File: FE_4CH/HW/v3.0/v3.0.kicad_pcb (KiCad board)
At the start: 4 copper layers, 72 x 26 mm, 158 parts, among them J1 SMA-ANG, J2 PINH_2MM_2P, J3 USB4080-03-A, J6 MS300-10F, U1 MAX2771, U10 74AVC9112DCH, U11 PI3USB302-AZBEX, U2 MAX2771, U3 MAX2771, U4 MAX2771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

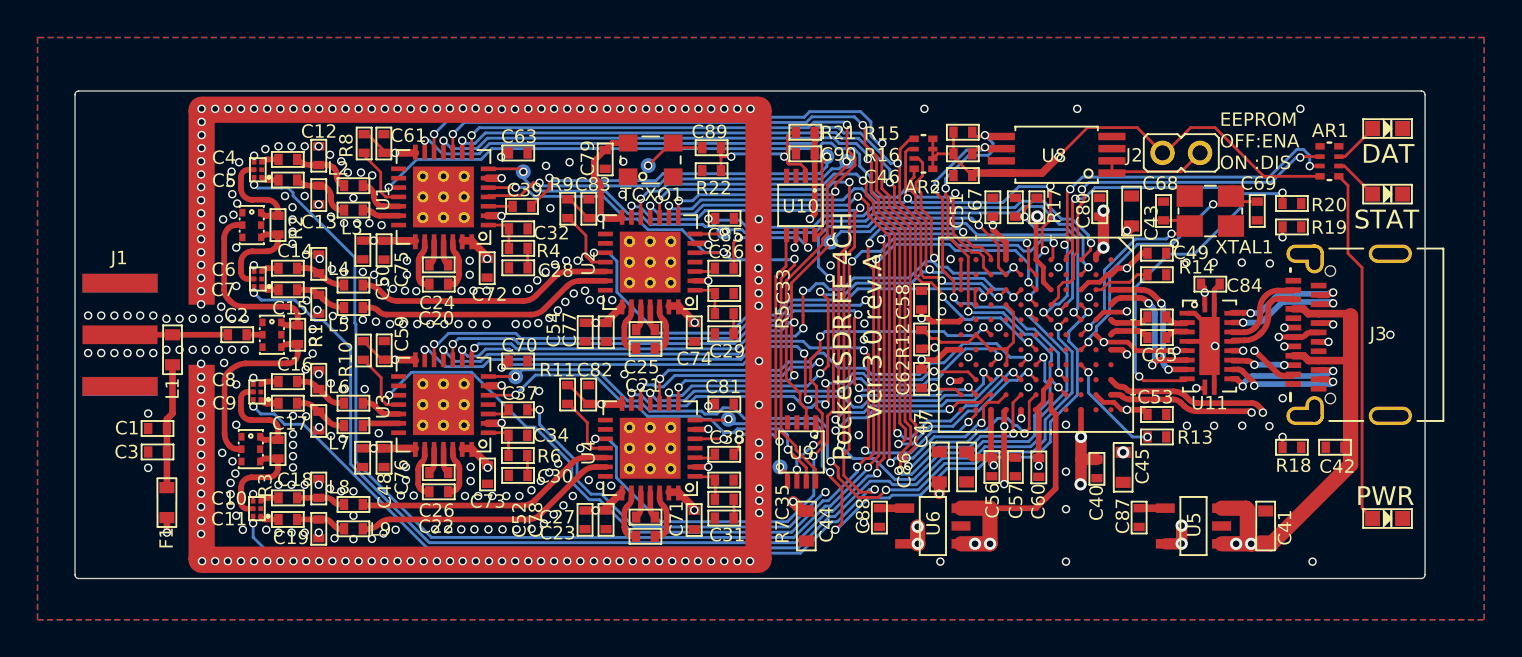
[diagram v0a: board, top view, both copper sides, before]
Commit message: replace wilkinson splitter with double, add mounting holes and fidushes
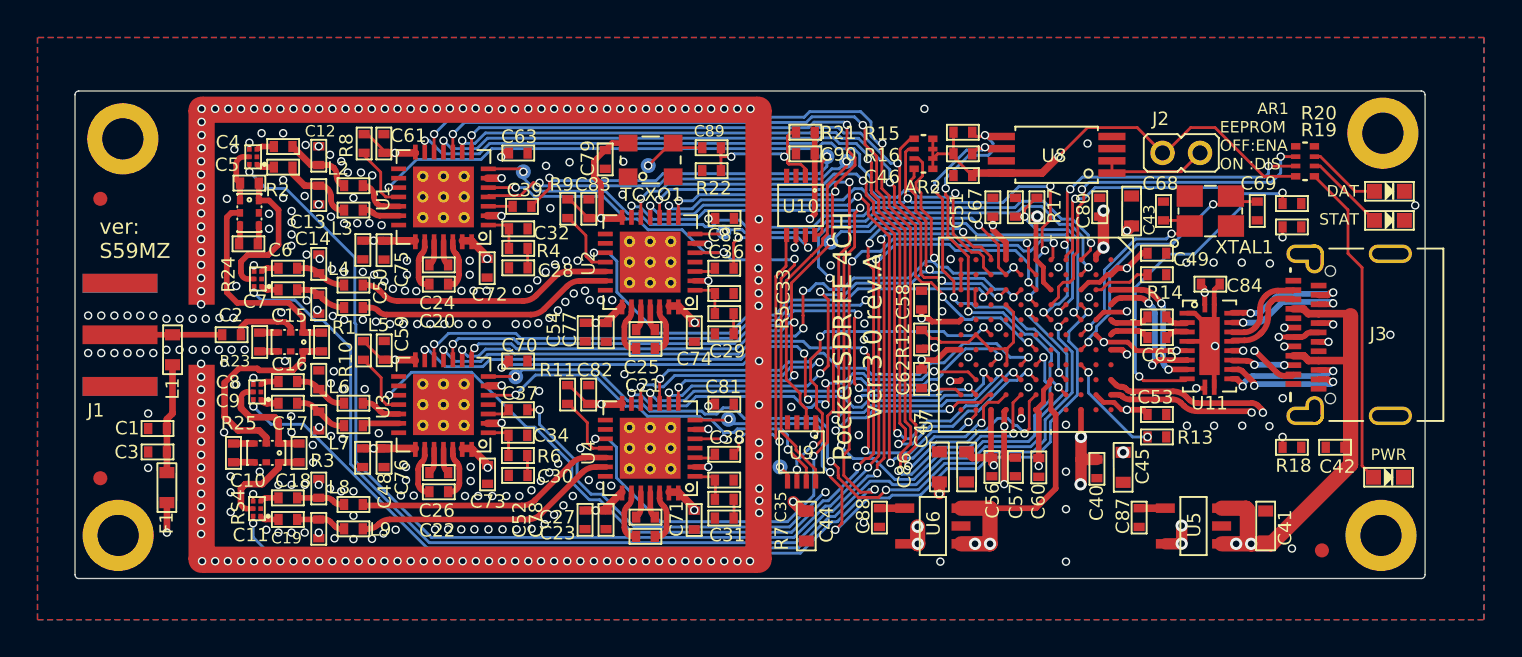
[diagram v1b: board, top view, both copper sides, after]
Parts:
- added FID1: Fiducial, Fiducial:Fiducial_0.75mm_Mask1.5mm, F.Cu at (122.4, 96.5)
- added FID2: Fiducial, Fiducial:Fiducial_0.75mm_Mask1.5mm, F.Cu at (122.4, 111.4)
- added FID3: Fiducial, Fiducial:Fiducial_0.75mm_Mask1.5mm, F.Cu at (187.5, 115.2)
- added H1: MountingHole_Pad, MountingHole:MountingHole_2.2mm_M2_DIN965_Pad, F.Cu at (123.6, 93.3)
- added H2: MountingHole_Pad, MountingHole:MountingHole_2.2mm_M2_DIN965_Pad, F.Cu at (123.3, 114.5)
- added H3: MountingHole_Pad, MountingHole:MountingHole_2.2mm_M2_DIN965_Pad, F.Cu at (190.7, 114.5)
- added H4: MountingHole_Pad, MountingHole:MountingHole_2.2mm_M2_DIN965_Pad, F.Cu at (190.8, 93.0)
- added R23: 100, pocket_sdr_v2.3:C1005, F.Cu at (130.9, 104.1)
- added R24: 100, pocket_sdr_v2.3:C1005, F.Cu at (130.3, 98.9)
- added R25: 100, pocket_sdr_v2.3:C1005, F.Cu at (129.5, 110.0)
- R1, R2, R3: value 100 -> 200
- RD1, RD2, RD3: value PD0922J5050S2HF -> PD0922J5050D2HF
- moved LED3 3.35 mm to (191.1, 96.1)
- moved R2 2.71 mm to (130.3, 95.7), turned to 180 degrees
- moved LED1 2.20 mm to (191.1, 111.3)
- moved LED2 1.40 mm to (191.1, 97.7)
- moved R1 1.33 mm to (134.2, 104.1)
- moved AR1 1.30 mm to (186.6, 94.5)
- moved R3 1.14 mm to (133.0, 110.0)
- moved RD1 1.07 mm to (132.5, 104.1), turned to 0 degrees
- moved RD3 0.85 mm to (131.2, 110.0), turned to 0 degrees
- moved F1 0.80 mm to (125.9, 111.9)
- moved C4 0.73 mm to (132.1, 93.7)
- moved C5 0.73 mm to (132.1, 94.8)
- moved RS1 0.73 mm to (130.5, 94.3)
- moved RD2 0.66 mm to (130.3, 97.2)
- moved C2 0.30 mm to (129.4, 103.8)
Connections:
- RD1 pad 1: GND -> Net-(R1-P$2)
- RD1 pad 3: GND -> Net-(R23-P$1)
- RD1 pad 4: Net-(R1-P$1) -> Net-(R23-P$2)
- RD1 pad 6: Net-(R1-P$2) -> Net-(R1-P$1)
- RD2 pad 1: GND -> Net-(R2-P$2)
- RD2 pad 3: GND -> Net-(R24-P$1)
- RD2 pad 4: Net-(R2-P$1) -> Net-(R24-P$2)
- RD2 pad 6: Net-(R2-P$2) -> Net-(R2-P$1)
- RD3 pad 1: GND -> Net-(R3-P$2)
- RD3 pad 3: GND -> Net-(R25-P$1)
- RD3 pad 4: Net-(R3-P$1) -> Net-(R25-P$2)
- RD3 pad 6: Net-(R3-P$2) -> Net-(R3-P$1)
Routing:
- net Net-(RD1-INPUT): track 0.85 -> 3.58 mm
- net Net-(R2-P$2): track 5.33 -> 2.84 mm
- net Net-(R2-P$1): track 5.31 -> 7.79 mm
- net /LED1: track 23.0 -> 20.8 mm
- net Net-(AR1-P3): track 2.42 -> 4.40 mm
- net +3.3V: track 280.6 -> 278.9 mm
- net Net-(AR1-P1): track 19.0 -> 17.4 mm
- net Net-(AR1-P5): track 2.44 -> 3.97 mm
- net Net-(R25-P$2): track 0.00 -> 1.19 mm
- net Net-(R25-P$1): track 0.00 -> 1.09 mm
- net Net-(R1-P$2): track 10.2 -> 11.2 mm
- net Net-(R23-P$2): track 0.00 -> 0.99 mm
- net Net-(R23-P$1): track 0.00 -> 0.99 mm
- net Net-(R24-P$2): track 0.00 -> 0.84 mm
- net Net-(R24-P$1): track 0.00 -> 0.84 mm
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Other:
- board text added: "ver: S59MZ"
- board text removed: "JLCJLCJLCJLC"
